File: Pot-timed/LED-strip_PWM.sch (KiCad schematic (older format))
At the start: 14 parts, among them IC1 MADW__ATTINY13-MM, P1 CONN_2, P2 CONN_2, T1 AO3400, U1 MCP1804-SOT23-5

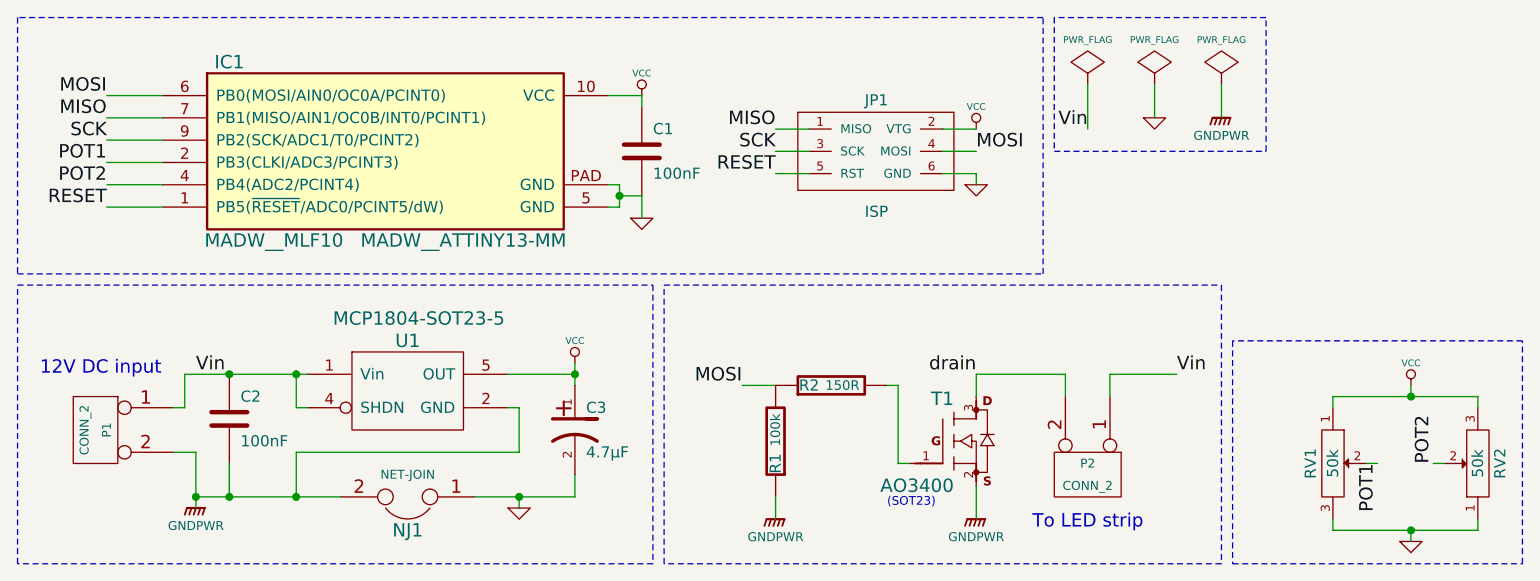
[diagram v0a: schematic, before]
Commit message: Pot-timed (single board): switched to ATtiny10 SOT23-6.
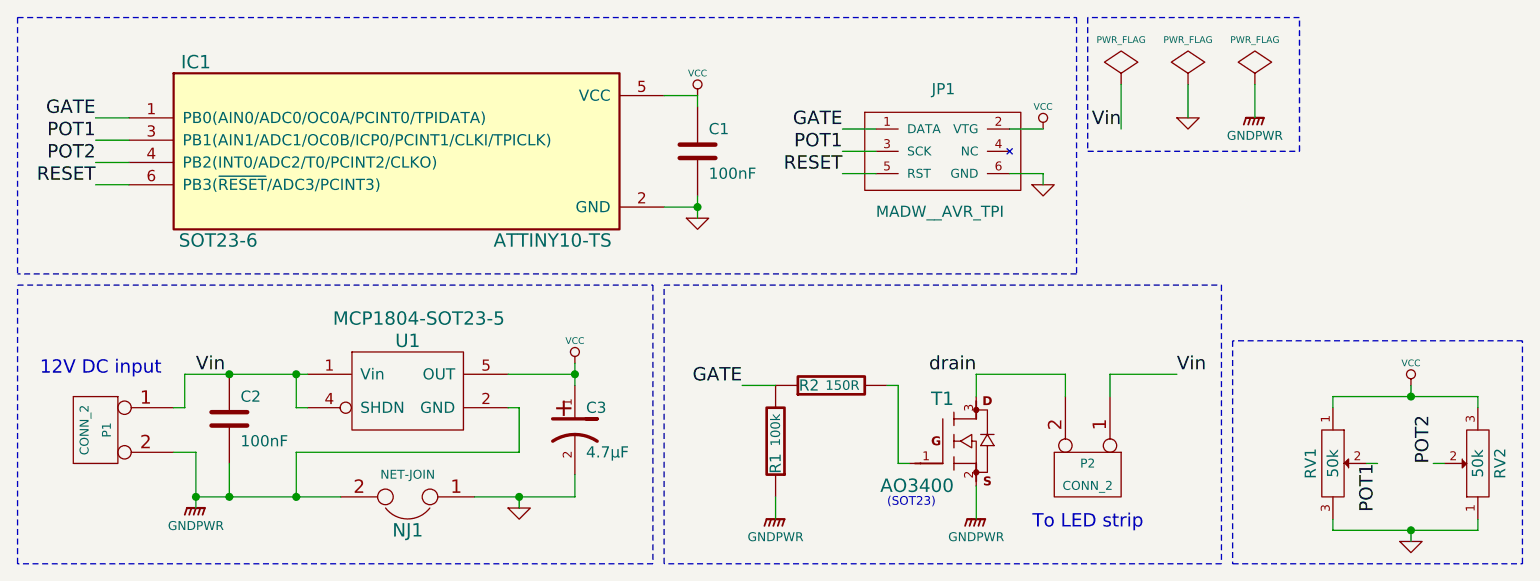
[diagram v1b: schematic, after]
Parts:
- removed IC1: MADW__ATTINY13-MM, MADW__MLF10, symbol MADW__ATTINY13-MM
- removed JP1: ISP, symbol MADW__AVR_ISP
- added IC1: ATTINY10-TS, SOT23-6, symbol ATTINY10-TS
- added JP1: MADW__AVR_TPI, symbol MADW__AVR_TPI
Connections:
- net GND: now also IC1.2 (GND), JP1.6 (GND)
- net POT1: now also IC1.3 (PB1(AIN1/ADC1/OC0B/ICP0/PCINT1/CLKI/TPICLK)), JP1.3 (SCK)
- net POT2: now also IC1.4 (PB2(INT0/ADC2/T0/PCINT2/CLKO))
- net RESET: now also IC1.6 (PB3(~RESET~/ADC3/PCINT3)), JP1.5 (RST)
- net VCC: now also IC1.5 (VCC), JP1.2 (VTG)
- net MOSI renamed GATE
- net GATE: now also IC1.1 (PB0(AIN0/ADC0/OC0A/PCINT0/TPIDATA)), JP1.1 (DATA)
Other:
- moved on the sheet: C1

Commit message: Revert "Pot-timed (single board): switched to ATtiny10 SOT23-6."
This reverts commit c61ef78eb5273ce0300997b1b0118eed30148325.

C + ATtiny10 not supported by avr-gcc
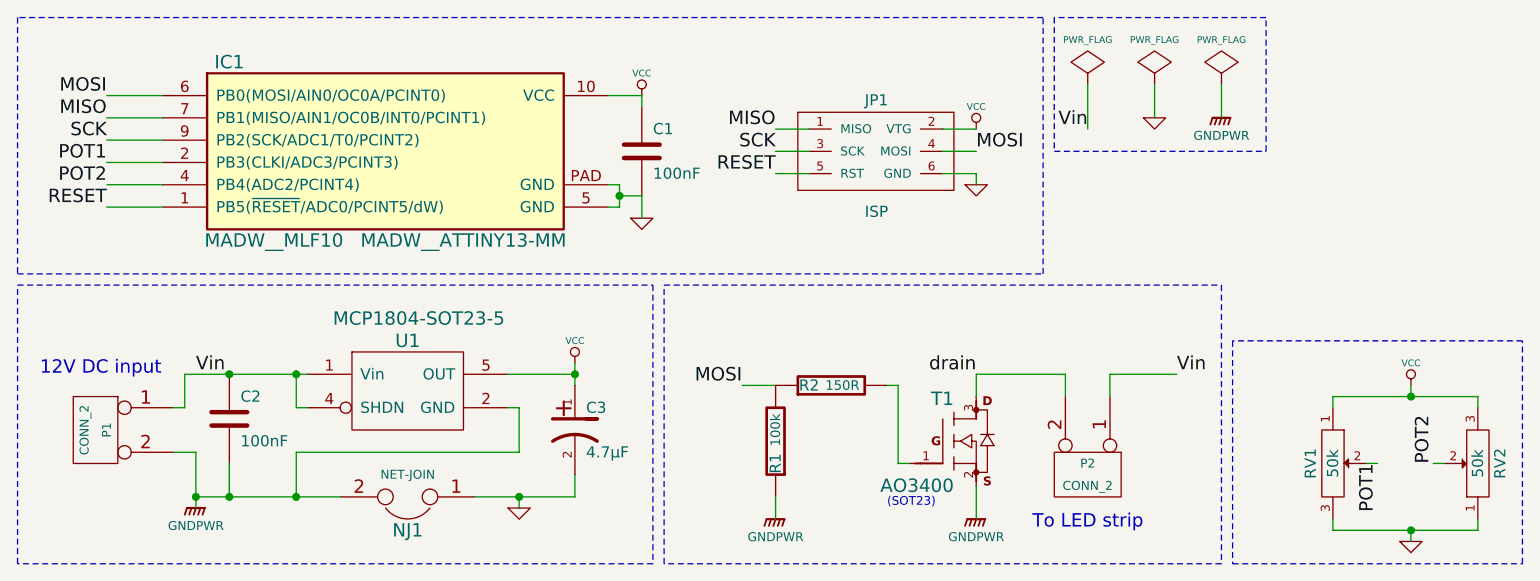
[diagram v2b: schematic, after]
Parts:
- removed IC1: ATTINY10-TS, SOT23-6, symbol ATTINY10-TS
- removed JP1: MADW__AVR_TPI, symbol MADW__AVR_TPI
- added IC1: MADW__ATTINY13-MM, MADW__MLF10, symbol MADW__ATTINY13-MM
- added JP1: ISP, symbol MADW__AVR_ISP
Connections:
- net GND: now also IC1.5 (GND), IC1.PAD (GND), JP1.6 (GND)
- net POT1: now also IC1.2 (PB3(CLKI/ADC3/PCINT3))
- net POT2: now also IC1.4 (PB4(ADC2/PCINT4))
- net RESET: now also IC1.1 (PB5(~RESET~/ADC0/PCINT5/dW)), JP1.5 (RST)
- net VCC: now also IC1.10 (VCC), JP1.2 (VTG)
- net GATE renamed MOSI
- net MOSI: now also IC1.6 (PB0(MOSI/AIN0/OC0A/PCINT0)), JP1.4 (MOSI)
- new net MISO: IC1.7 (PB1(MISO/AIN1/OC0B/INT0/PCINT1)), JP1.1 (MISO)
- new net SCK: IC1.9 (PB2(SCK/ADC1/T0/PCINT2)), JP1.3 (SCK)
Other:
- moved on the sheet: C1
